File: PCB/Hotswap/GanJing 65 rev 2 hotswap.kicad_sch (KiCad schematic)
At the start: 141 parts, among them SW1 EC11_rotary_encoder, U1 Elite-C

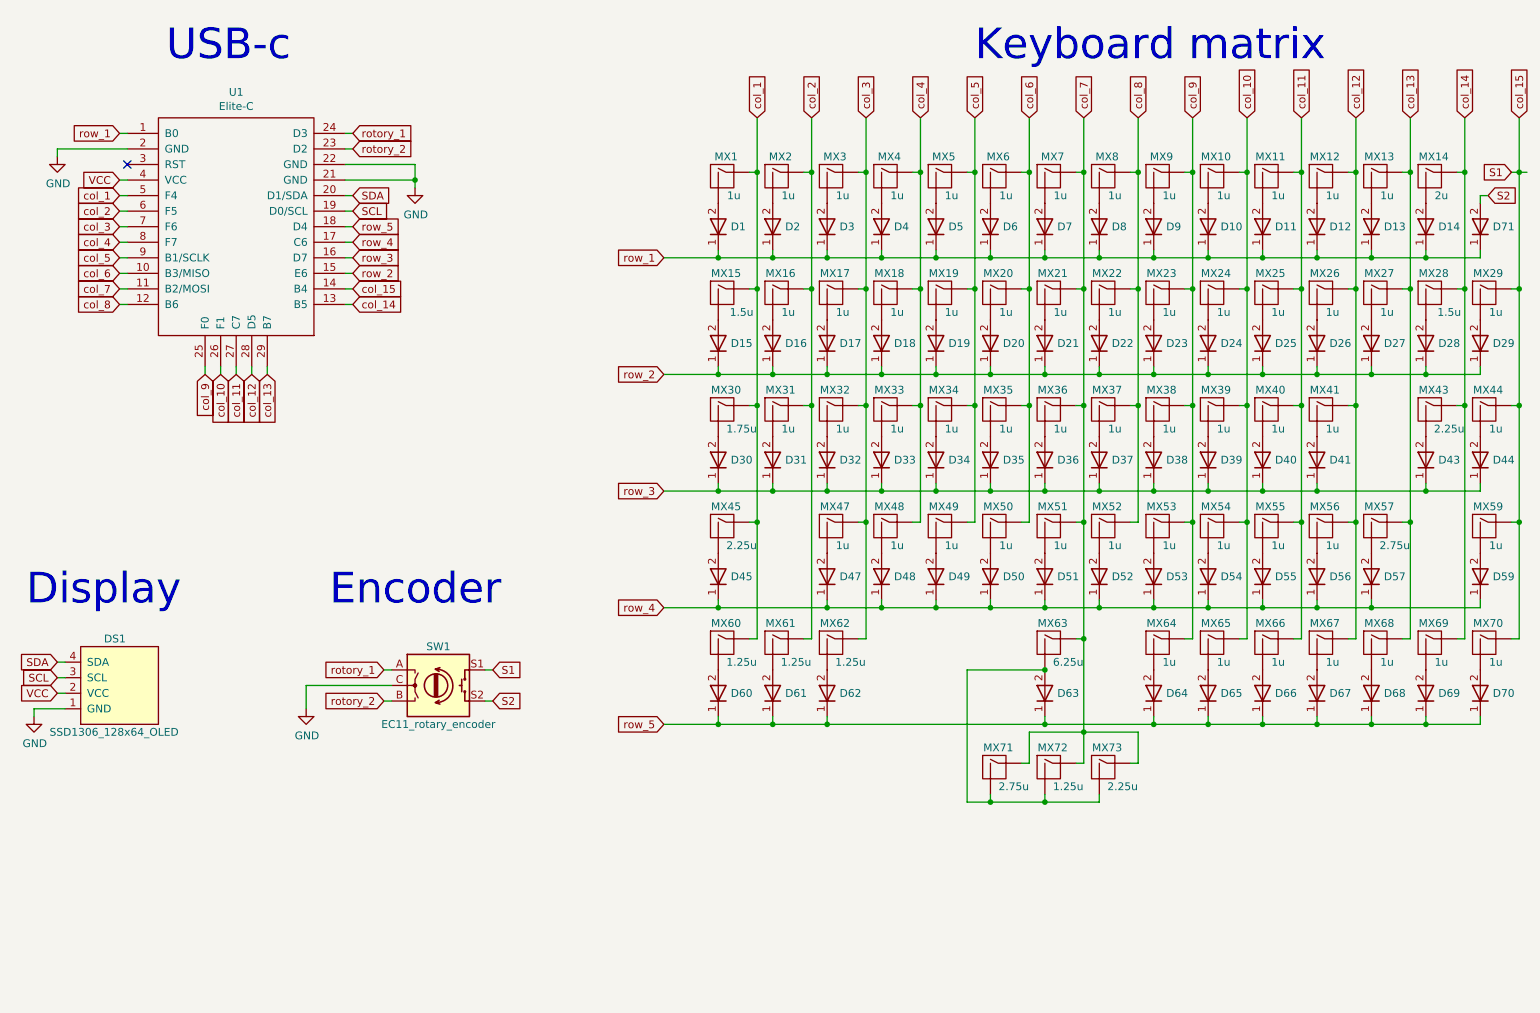
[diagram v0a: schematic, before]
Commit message: Adding a bunch of different layout options to the hotswap board
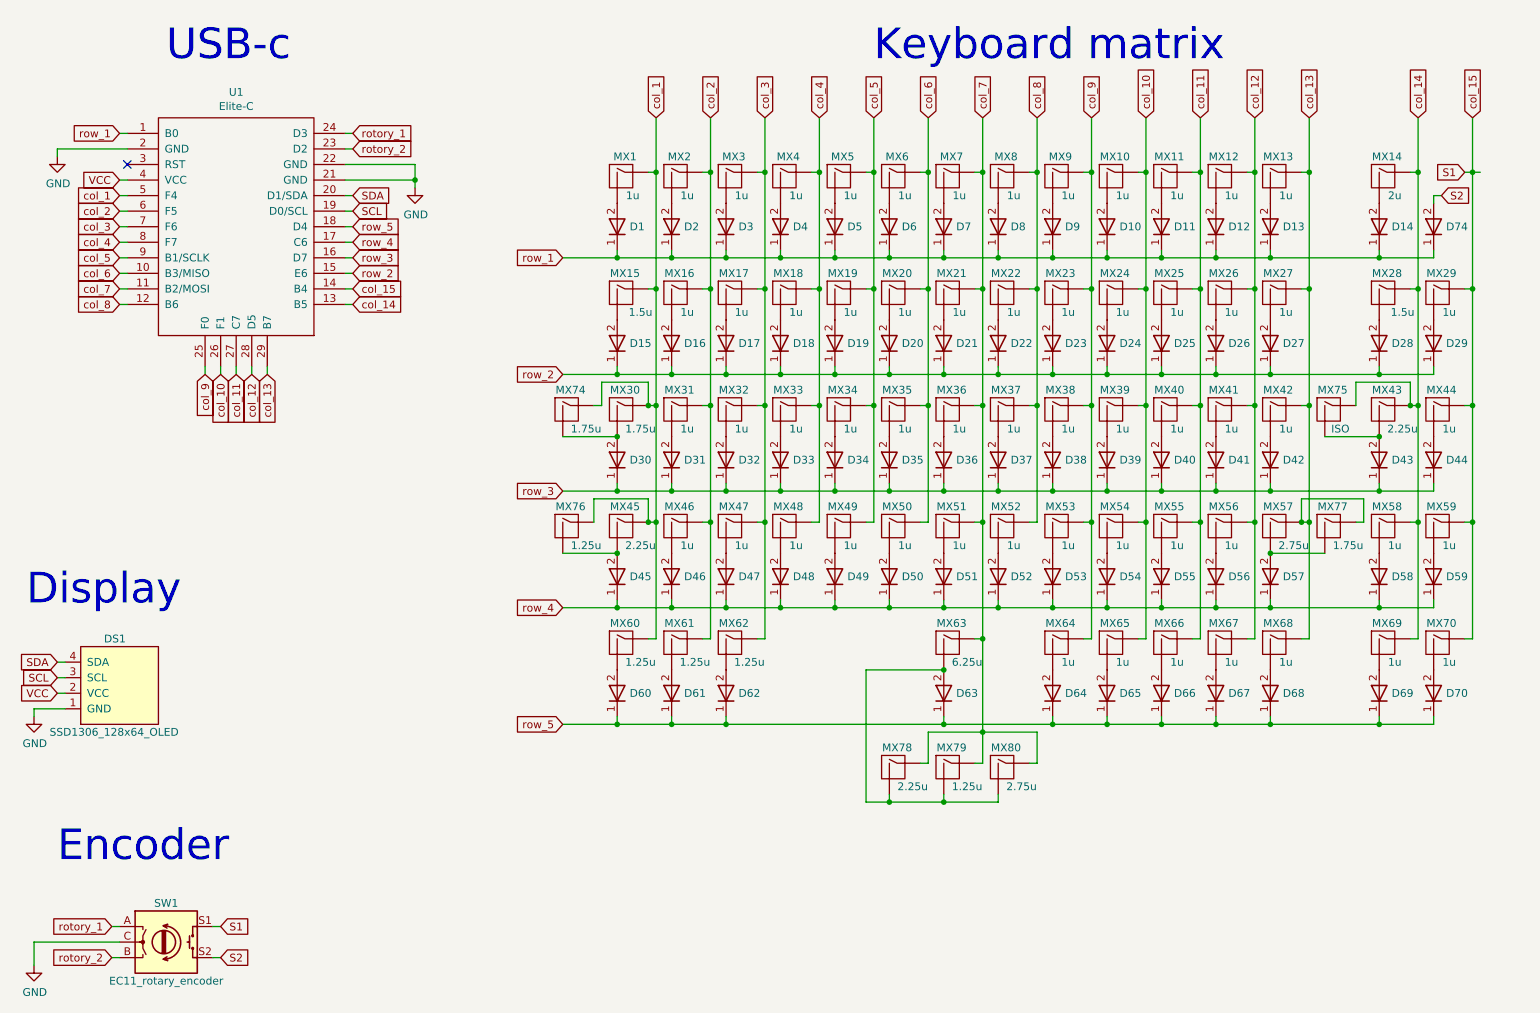
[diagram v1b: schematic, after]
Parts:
- removed MX71: MX_2.75u_no_LED_flipped_stabs, GanJing_components:MX_2.75u_no_LED_hotswap_flipped_stabs, symbol GanJing_components:MX_2.75u_no_LED_flipped_stabs
- removed MX73: MX_2.25u_no_LED_flipped_stabs, GanJing_components:MX_2.25u_no_LED_hotswap_flipped_stabs, symbol GanJing_components:MX_2.25u_no_LED_flipped_stabs
- added D42, D46, D58: 1N4148TR_diode, GanJing_components:1N4148TR_diode, symbol GanJing_components:1N4148TR_diode
- added MX42, MX46, MX58: MX_1u_no_LED, GanJing_components:MX_1u_no_LED_hotswap, symbol GanJing_components:MX_1u_no_LED
- added MX74: MX_1.75u_no_LED, GanJing_components:MX_1.75u_stepped_no_LED_hotswap, symbol GanJing_components:MX_1.75u_no_LED
- added MX75: MX_ISO_no_LED_flipped_stabs, GanJing_components:MX_ISO_no_LED_hotswap_flipped_stabs, symbol GanJing_components:MX_ISO_no_LED_flipped_stabs
- added MX76: MX_1.25u_no_LED, GanJing_components:MX_1.25u_no_LED_hotswap, symbol GanJing_components:MX_1.25u_no_LED
- added MX77: MX_1.75u_no_LED, GanJing_components:MX_1.75u_no_LED_hotswap, symbol GanJing_components:MX_1.75u_no_LED
- added MX78: MX_2.25u_no_LED_flipped_stabs, GanJing_components:MX_2.25u_no_LED_hotswap_flipped_stabs, symbol GanJing_components:MX_2.25u_no_LED_flipped_stabs
- added MX80: MX_2.75u_no_LED_flipped_stabs, GanJing_components:MX_2.75u_no_LED_hotswap_flipped_stabs, symbol GanJing_components:MX_2.75u_no_LED_flipped_stabs
- renumbered D71 to D74, MX72 to MX79
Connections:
- net col_1: now also MX74.1 (COL), MX76.1 (COL)
- net col_13: now also MX42.1 (COL), MX77.1 (COL)
- net col_14: now also MX58.1 (COL), MX75.1 (COL)
- net col_2: now also MX46.1 (COL)
- net col_7: now also MX78.1 (COL), MX80.1 (COL)
- net row_3: now also D42.1
- net row_4: now also D46.1, D58.1
- net at D30.2, MX30.2 (ROW): now also MX74.2 (ROW)
- net at D45.2, MX45.2 (ROW): now also MX76.2 (ROW)
- net at D63.2, MX63.2 (ROW), MX79.2 (ROW): now also MX78.2 (ROW), MX80.2 (ROW)
- net at D43.2, MX43.2 (ROW): now also MX75.2 (ROW)
- net at D57.2, MX57.2 (ROW): now also MX77.2 (ROW)
- new net: D46.2, MX46.2 (ROW)
- new net: D58.2, MX58.2 (ROW)
- new net: D42.2, MX42.2 (ROW)
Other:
- moved on the sheet: D1, D10, D11, D12, D13, D14, D15, D16, D17, D18, D19, D2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

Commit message: Updating PCB and firmware
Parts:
- added D63, D64, D66: 1N4148TR_diode, GanJing_components:1N4148TR_diode, symbol GanJing_components:1N4148TR_diode
- renumbered D63 to D65, D64 to D67, D65 to D68, D66 to D69, D67 to D70, D68 to D71, D69 to D72, D70 to D73, MX78 to MX63, MX79 to MX64, MX63 to MX65, MX80 to MX66, MX64 to MX67, MX65 to MX68, MX66 to MX69, MX67 to MX70, MX68 to MX71, MX69 to MX72, MX70 to MX73
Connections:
- net col_5: now also MX63.1 (COL)
- net col_6: now also MX64.1 (COL)
- net col_7: no longer MX63.1 (COL), MX64.1 (COL), MX66.1 (COL)
- net col_8: now also MX66.1 (COL)
- net row_5: now also D63.1, D64.1, D66.1
- new net: D65.2, MX65.2 (ROW)
- new net: D64.2, MX64.2 (ROW)
- new net: D63.2, MX63.2 (ROW)
- new net: D66.2, MX66.2 (ROW)
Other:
- moved on the sheet: MX63, MX64, MX66

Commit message: Adding 3d models and flipping the right shift stabilizers to reduce interference
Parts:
- MX1, MX10, MX11, MX12, MX13, MX2, MX3, MX4, MX46, MX5, MX6, MX7, MX8, MX9: footprint GanJing_components:MX_1u_no_LED_hotswap -> GanJing_components:MX_1u_no_LED_hotswap_flipped_pins
- MX28: footprint GanJing_components:MX_1.5u_no_LED_hotswap -> GanJing_components:MX_1.5u_no_LED_hotswap_rotated
- MX43: footprint GanJing_components:MX_2.25u_no_LED_hotswap -> GanJing_components:MX_2.25u_no_LED_hotswap_rotated_flipped_stabs

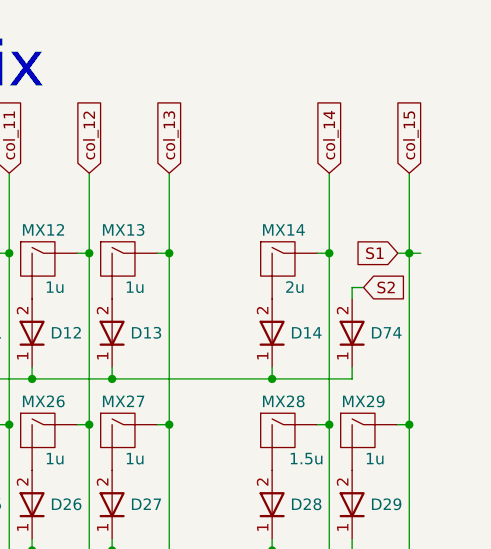
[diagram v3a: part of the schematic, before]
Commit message: Adding option to have switch instead of knob
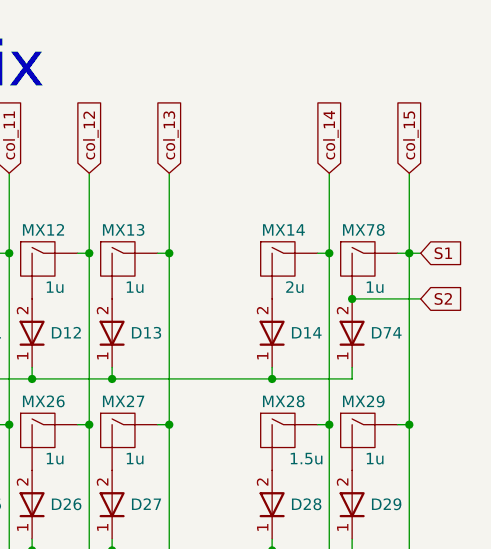
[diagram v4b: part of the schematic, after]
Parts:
- added MX78: MX_1u_no_LED, GanJing_components:MX_1u_no_LED_hotswap, symbol GanJing_components:MX_1u_no_LED
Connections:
- net S1: now also MX78.1 (COL)
- net S2: now also MX78.2 (ROW)
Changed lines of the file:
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@@
   (junction (at 259.08 104.14) (diameter 0) (color 0 0 0 0)
   )
+  (junction (at 252.73 52.07) (diameter 0) (color 0 0 0 0)
+  )
   (junction (at 231.14 104.14) (diameter 0) (color 0 0 0 0)
   )
@@
     (stroke (width 0) (type default) (color 0 0 0 0))
   )
-  (wire (pts (xy 252.73 52.07) (xy 252.73 50.8))
-    (stroke (width 0) (type default) (color 0 0 0 0))
-  )
   (wire (pts (xy 250.19 85.09) (xy 250.19 104.14))
     (stroke (width 0) (type default) (color 0 0 0 0))
@@
     (stroke (width 0) (type default) (color 0 0 0 0))
   )
+  (wire (pts (xy 259.08 46.99) (xy 260.35 46.99))
+    (stroke (width 0) (type default) (color 0 0 0 0))
+  )
   (wire (pts (xy 186.69 123.19) (xy 187.96 123.19))
     (stroke (width 0) (type default) (color 0 0 0 0))
@@
     (stroke (width 0) (type default) (color 0 0 0 0))
   )
-  (wire (pts (xy 259.08 46.99) (xy 260.35 46.99))
-    (stroke (width 0) (type default) (color 0 0 0 0))
-  )
   (wire (pts (xy 163.83 135.89) (xy 163.83 137.16))
     (stroke (width 0) (type default) (color 0 0 0 0))
@@
     (stroke (width 0) (type default) (color 0 0 0 0))
   )
-  (wire (pts (xy 252.73 50.8) (xy 254 50.8))
-    (stroke (width 0) (type default) (color 0 0 0 0))
-  )
   (wire (pts (xy 205.74 85.09) (xy 205.74 66.04))
     (stroke (width 0) (type default) (color 0 0 0 0))
@@
     (stroke (width 0) (type default) (color 0 0 0 0))
   )
+  (wire (pts (xy 252.73 52.07) (xy 260.35 52.07))
+    (stroke (width 0) (type default) (color 0 0 0 0))
+  )
   (wire (pts (xy 161.29 46.99) (xy 161.29 66.04))
     (stroke (width 0) (type default) (color 0 0 0 0))
@@
     )
   )
+  (global_label "S1" (shape input) (at 260.35 46.99 0) (fields_autoplaced)
+    (effects (font (size 1.27 1.27)) (justify left))
+    (property "Intersheet References" "${INTERSHEET_REFS}" (id 0) (at 525.78 93.98 0)
+      (effects (font (size 1.27 1.27)) hide)
+    )
+  )
   (global_label "col_15" (shape input) (at 259.08 38.1 90) (fields_autoplaced)
     (effects (font (size 1.27 1.27)) (justify left))
@@
     )
   )
-  (global_label "S2" (shape input) (at 254 50.8 0) (fields_autoplaced)
+  (global_label "S2" (shape input) (at 260.35 52.07 0) (fields_autoplaced)
     (effects (font (size 1.27 1.27)) (justify left))
-    (property "Intersheet References" "${INTERSHEET_REFS}" (id 0) (at -7.62 0 0)
+    (property "Intersheet References" "${INTERSHEET_REFS}" (id 0) (at -1.27 1.27 0)
       (effects (font (size 1.27 1.27)) hide)
     )
@@
     )
   )
-  (global_label "S1" (shape input) (at 257.81 46.99 180) (fields_autoplaced)
-    (effects (font (size 1.27 1.27)) (justify right))
-    (property "Intersheet References" "${INTERSHEET_REFS}" (id 0) (at -7.62 0 0)
-      (effects (font (size 1.27 1.27)) hide)
-    )
-  )
   (global_label "rotory_1" (shape input) (at 36.83 170.18 180) (fields_autoplaced)
     (effects (font (size 1.27 1.27)) (justify right))
@@
     (pin "2")
   )
+  (symbol (lib_id "GanJing_components:MX_1u_no_LED") (at 252.73 46.99 0) (unit 1)
+    (in_bom yes) (on_board yes)
+    (property "Reference" "MX78" (id 0) (at 254 44.45 0))
+    (property "Value" "MX_1u_no_LED" (id 1) (at 252.73 46.99 0)
+      (effects (font (size 1.27 1.27)) hide)
+    )
+    (property "Footprint" "GanJing_components:MX_1u_no_LED_hotswap" (id 2) (at 252.73 46.99 0)
+      (effects (font (size 1.27 1.27)) hide)
+    )
+    (property "Datasheet" "https://datasheet.octopart.com/MX1A-11NW-Cherry-datasheet-34676.pdf" (id 3) (at 252.73 46.99 0)
+      (effects (font (size 1.27 1.27)) hide)
+    )
+    (property "Size" "1u" (id 4) (at 255.27 50.8 0))
+    (pin "1")
+    (pin "2")
+  )
   (symbol (lib_id "GanJing_components:MX_1u_no_LED") (at 226.06 85.09 0) (unit 1)
     (in_bom yes) (on_board yes)
@@
       (reference "MX77") (unit 1) (value "MX_1.75u_no_LED") (footprint "GanJing_components:MX_1.75u_no_LED_hotswap")
     )
+    (path "/b09903a5-693f-4dec-87b4-b28ce4c6d7db"
+      (reference "MX78") (unit 1) (value "MX_1u_no_LED") (footprint "GanJing_components:MX_1u_no_LED_hotswap")
+    )
     (path "/00000000-0000-0000-0000-000062183c25"

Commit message: Updating soldered version
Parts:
- renumbered D74 to D15, D15 to D16, D16 to D17, D17 to D18, D18 to D19, D19 to D20, D20 to D21, D21 to D22, D22 to D23, D23 to D24, D24 to D25, D25 to D26, D26 to D27, D27 to D28, D28 to D29, D29 to D30, D30 to D31, D31 to D32, D32 to D33, D33 to D34, D34 to D35, D35 to D36, D36 to D37, D37 to D38, D38 to D39, D39 to D40, D40 to D41, D41 to D42, D42 to D43, D43 to D44, D44 to D45, D45 to D46, D46 to D47, D47 to D48, D48 to D49, D49 to D50, D50 to D51, D51 to D52, D52 to D53, D53 to D54, D54 to D55, D55 to D56, D56 to D57, D57 to D58, D58 to D59, D59 to D60, D60 to D61, D61 to D62, D62 to D63, D63 to D64, D64 to D65, D65 to D66, D66 to D67, D67 to D68, D68 to D69, D69 to D70, D70 to D71, D71 to D72, D72 to D73, D73 to D74, MX78 to MX15, MX15 to MX16, MX16 to MX17, MX17 to MX18, MX18 to MX19, MX19 to MX20, MX20 to MX21, MX21 to MX22, MX22 to MX23, MX23 to MX24, MX24 to MX25, MX25 to MX26, MX26 to MX27, MX27 to MX28, MX28 to MX29, MX29 to MX30, MX30 to MX31, MX31 to MX32, MX32 to MX33, MX33 to MX34, MX34 to MX35, MX35 to MX36, MX36 to MX37, MX37 to MX38, MX38 to MX39, MX39 to MX40, MX40 to MX41, MX41 to MX42, MX42 to MX43, MX43 to MX44, MX44 to MX45, MX45 to MX46, MX46 to MX47, MX47 to MX48, MX48 to MX49, MX49 to MX50, MX50 to MX51, MX51 to MX52, MX52 to MX53, MX53 to MX54, MX54 to MX55, MX55 to MX56, MX56 to MX57, MX57 to MX58, MX58 to MX59, MX59 to MX60, MX60 to MX61, MX61 to MX62, MX62 to MX63, MX63 to MX64, MX64 to MX65, MX65 to MX66, MX66 to MX67, MX67 to MX68, MX68 to MX69, MX69 to MX70, MX70 to MX71, MX71 to MX72, MX72 to MX73, MX73 to MX74, MX74 to MX75, MX75 to MX76, MX76 to MX77, MX77 to MX78
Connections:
- net S1 renamed col_15
